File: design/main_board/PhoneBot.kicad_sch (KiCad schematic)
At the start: 37 parts, among them J101 CX70M-24P1, J102 AVR-ISP-6, J103 Conn_02x03_Odd_Even, J104 Conn_02x03_Odd_Even, J105 Conn_02x03_Odd_Even, J106 Conn_02x03_Odd_Even, U101 ATmega32U4-AU, Y101 ABM3-8.000MHZ-D2Y-T

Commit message: Created esp32 footprint and symbol
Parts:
- added U1: ESP32-S3-WROOM-1-N16R8, CustomFootprints:XCVR_ESP32-S3-WROOM-1-N16R8, symbol Custom:ESP32-S3-WROOM-1-N16R8
- R108: value 1k -> 1M; Part https://www.digikey.com/product-detail/en/yageo/RC0603JR-07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 -> https://www.digikey.com/en/products/detail/yageo/RC0603JR-0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
- R109: value 3.6k -> 3.6M; Part https://www.digikey.com/product-detail/en/yageo/RC0402JR-07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 -> https://www.digikey.com/en/products/detail/yageo/RC0603JR-0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
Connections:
- net +3V3: now also U1.2 (3V3), U1.3 (EN)
- net GND: now also U1.1 (GND), U1.40 (GND), U1.41_1 (GND), U1.41_2 (GND), U1.41_3 (GND), U1.41_4 (GND), U1.41_5 (GND), U1.41_6 (GND), U1.41_7 (GND), U1.41_8 (GND), U1.41_9 (GND)
- net ~BLE_RST renamed ~{BLE_RST}
- net ~RST renamed ~{RST}
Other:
- sheet BLESheet ports: added ~{BLE_RST}; removed ~BLE_RST

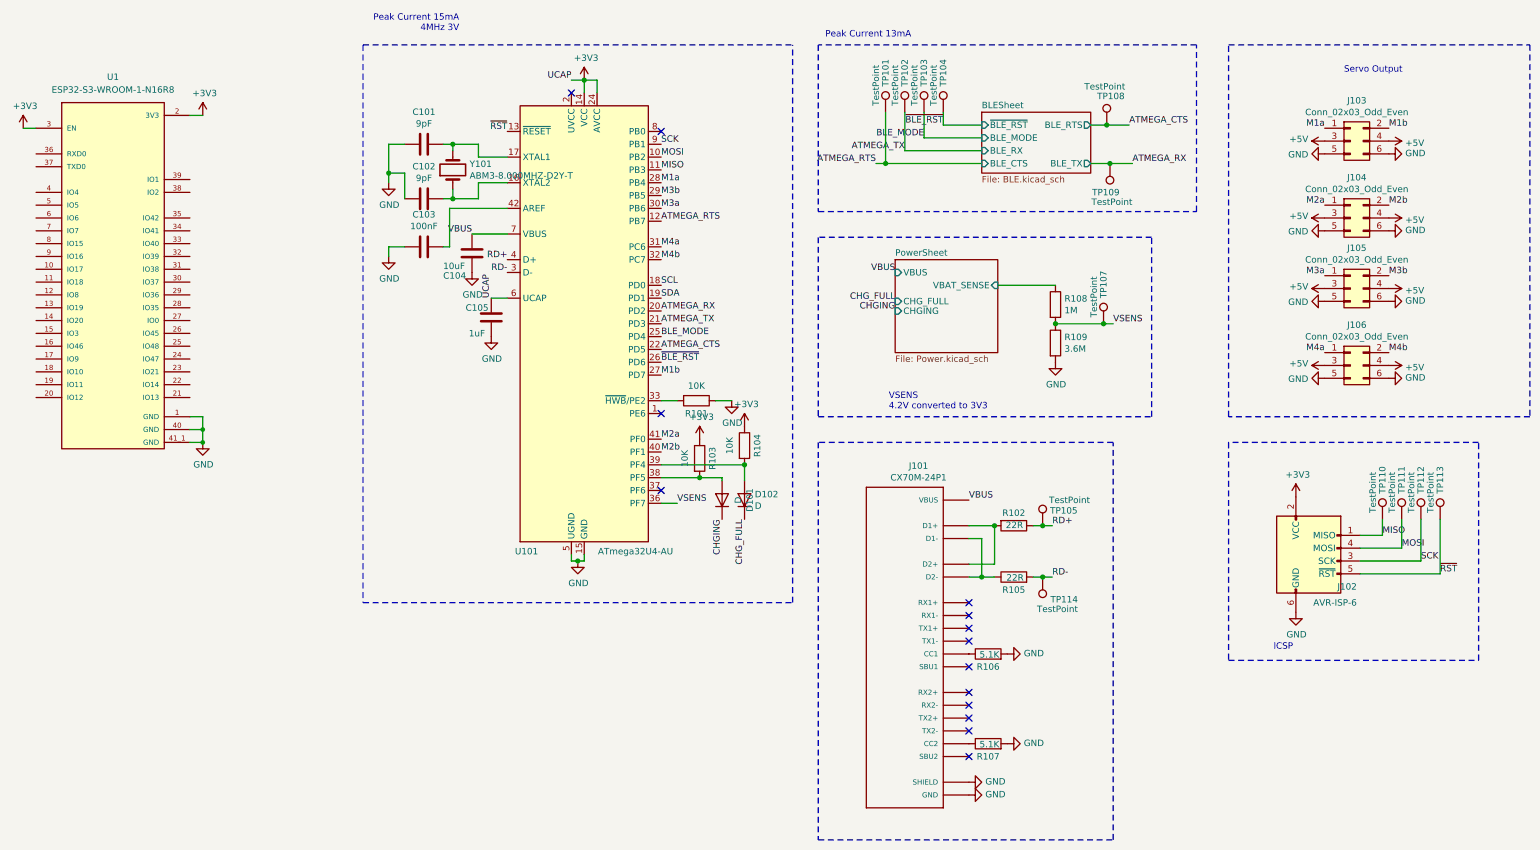
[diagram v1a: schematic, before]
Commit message: Schematic almost finished
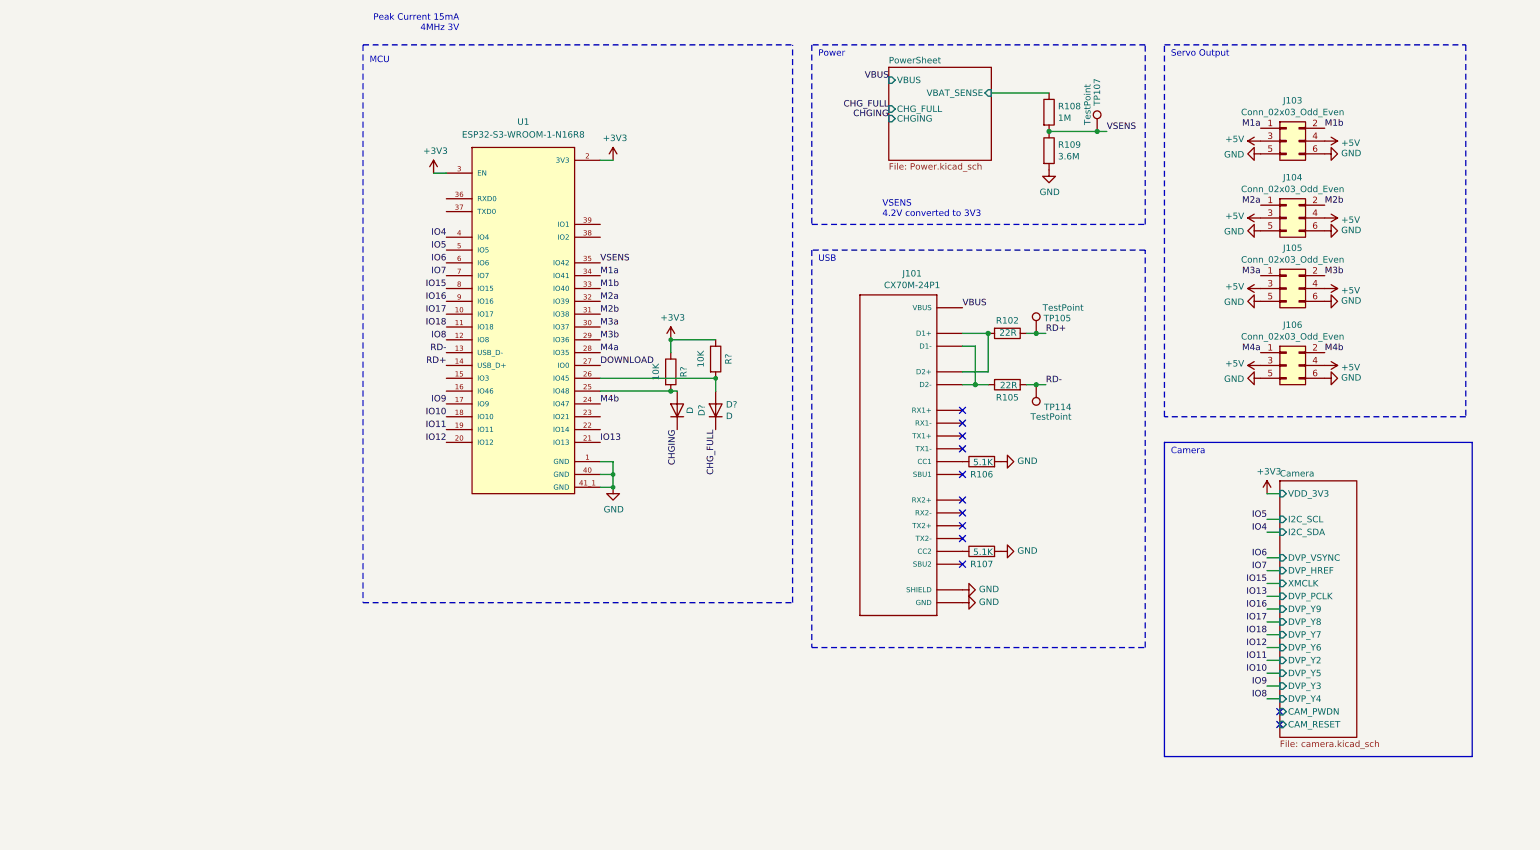
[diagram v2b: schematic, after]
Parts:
- removed C101, C102: 9pF, Capacitor_SMD:C_0603_1608Metric, symbol Device:C
- removed C103: 100nF, Capacitor_SMD:C_0603_1608Metric, symbol Device:C
- removed C104: 10uF, Capacitor_SMD:C_0603_1608Metric, symbol Device:C
- removed C105: 1uF, Capacitor_SMD:C_0603_1608Metric, symbol Device:C
- removed D101, D102: D, Diode_SMD:D_0603_1608Metric, symbol Device:D
- removed J102: AVR-ISP-6, Connector_PinHeader_2.54mm:PinHeader_2x03_P2.54mm_Vertical, symbol PhoneBot-rescue:AVR-ISP-6-Connector-PhoneBot-rescue
- removed R101, R103, R104: 10K, Resistor_SMD:R_0603_1608Metric, symbol Device:R
- removed TP101, TP102, TP103, TP104, TP108, TP109, TP110, TP111, TP112, TP113: TestPoint, TestPoint:TestPoint_Pad_D1.0mm, symbol Connector:TestPoint
- removed U101: ATmega32U4-AU, Package_QFP:TQFP-44_10x10mm_P0.8mm, symbol PhoneBot-rescue:ATmega32U4-AU-MCU_Microchip_ATmega-PhoneBot-rescue-PhoneBot-res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
- removed Y101: ABM3-8.000MHZ-D2Y-T, Crystal:Crystal_SMD_Abracon_ABM3-2Pin_5.0x3.2mm, symbol Device:Crystal
- added D? (x2): D, Diode_SMD:D_0603_1608Metric, symbol Device:D
- added R? (x2): 10K, Resistor_SMD:R_0603_1608Metric, symbol Device:R
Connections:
- net +3V3: now also R?.1, R?.1
- net CHGING: now also D?.1 (K)
- net CHG_FULL: now also D?.1 (K)
- net M1a: now also U1.34 (IO41)
- net M1b: now also U1.33 (IO40)
- net M2a: now also U1.32 (IO39)
- net M2b: now also U1.31 (IO38)
- net M3a: now also U1.30 (IO37)
- net M3b: now also U1.29 (IO36)
- net M4a: now also U1.28 (IO35)
- net M4b: now also U1.24 (IO47)
- net RD+: now also U1.14 (IO20)
- net RD-: now also U1.13 (IO19)
- net VSENS: now also U1.35 (IO42)
- net IO17: now reaches U1.10 (IO17)
- net IO18: now reaches U1.11 (IO18)
- net IO8: now reaches U1.12 (IO8)
- net IO9: now reaches U1.17 (IO9)
- net IO10: now reaches U1.18 (IO10)
- net IO11: now reaches U1.19 (IO11)
- net IO12: now reaches U1.20 (IO12)
- net IO13: now reaches U1.21 (IO13)
- net at U1.25 (IO48): now also D?.2 (A), R?.2
- net at U1.26 (IO45): now also D?.2 (A), R?.2
- net DOWNLOAD: now reaches U1.27 (IO0)
- net IO4: now reaches U1.4 (IO4)
- net IO5: now reaches U1.5 (IO5)
- net IO6: now reaches U1.6 (IO6)
- net IO7: now reaches U1.7 (IO7)
- net IO15: now reaches U1.8 (IO15)
- net IO16: now reaches U1.9 (IO16)
- no-connect marks 14 -> 12
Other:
- removed sheet BLESheet
- added sheet Camera (camera.kicad_sch)
- note added: "Camera"
- note added: "MCU"
- note added: "Power"
- note added: "USB"
- note removed: "ICSP"
- note removed: "Peak Current 13mA"
- moved on the sheet: J101, J103, J104, J105, J106, R102, R105, R106, R107, R108, R109, TP105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

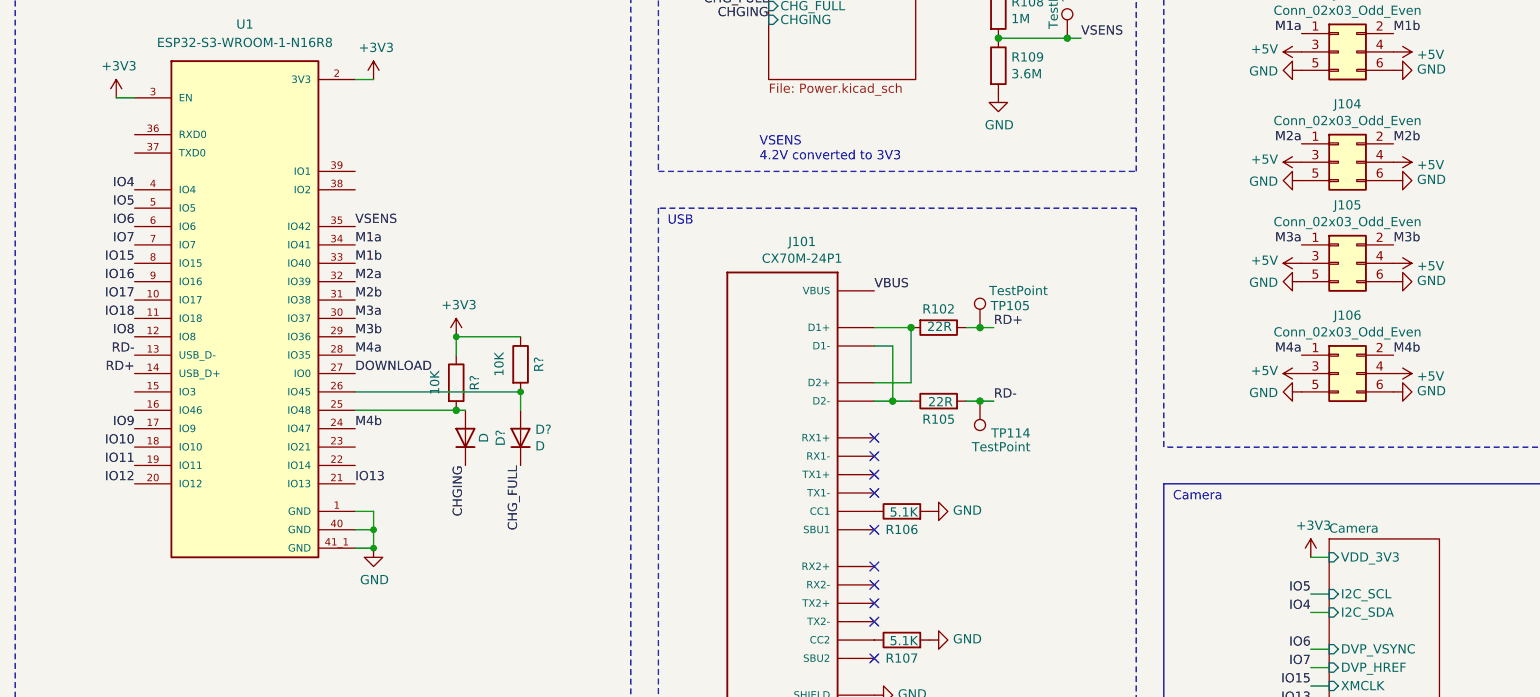
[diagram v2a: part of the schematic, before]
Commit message: Added new firmware hello world for ESP32-S3
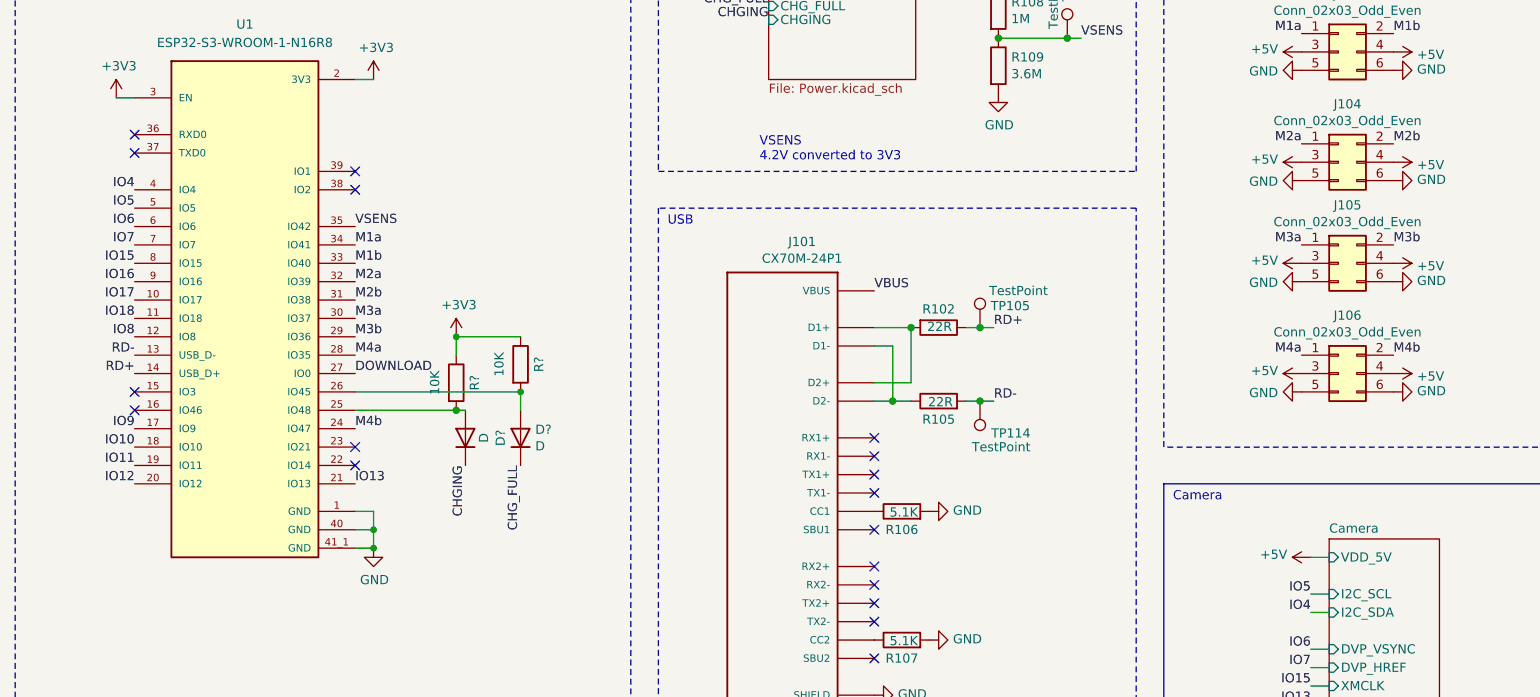
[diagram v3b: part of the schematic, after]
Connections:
- no-connect marks 12 -> 20
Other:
- sheet Camera ports: added VDD_5V; removed VDD_3V3
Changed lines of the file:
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@@
   (no_connect (at 137.795 127))
   (no_connect (at 137.795 114.3))
+  (no_connect (at 66.04 97.79))
+  (no_connect (at 66.04 100.33))
+  (no_connect (at 35.56 90.17))
+  (no_connect (at 35.56 92.71))
+  (no_connect (at 35.56 57.15))
+  (no_connect (at 35.56 54.61))
+  (no_connect (at 66.04 62.23))
+  (no_connect (at 66.04 59.69))
   (no_connect (at 137.795 104.14))
   (no_connect (at 137.795 96.52))
@@
     (pin "2")
   )
-  (symbol (lib_id "power:+3V3") (at 198.12 113.03 0) (unit 1)
-    (in_bom yes) (on_board yes)
-    (property "Reference" "#PWR?" (id 0) (at 198.12 116.84 0)
-      (effects (font (size 1.27 1.27)) hide)
-    )
-    (property "Value" "+3V3" (id 1) (at 198.501 108.6358 0))
-    (property "Footprint" "" (id 2) (at 198.12 113.03 0)
-      (effects (font (size 1.27 1.27)) hide)
-    )
-    (property "Datasheet" "" (id 3) (at 198.12 113.03 0)
-      (effects (font (size 1.27 1.27)) hide)
-    )
-    (pin "1")
-  )
   (symbol (lib_id "Device:D") (at 81.28 96.52 90) (unit 1)
     (in_bom yes) (on_board yes)
@@
     )
     (property "Datasheet" "" (id 3) (at 33.02 49.53 0)
+      (effects (font (size 1.27 1.27)) hide)
+    )
+    (pin "1")
+  )
+  (symbol (lib_id "power:+5V") (at 198.12 113.03 90) (unit 1)
+    (in_bom yes) (on_board yes)
+    (property "Reference" "#PWR?" (id 0) (at 201.93 113.03 0)
+      (effects (font (size 1.27 1.27)) hide)
+    )
+    (property "Value" "+5V" (id 1) (at 194.8688 112.649 90)
+      (effects (font (size 1.27 1.27)) (justify left))
+    )
+    (property "Footprint" "" (id 2) (at 198.12 113.03 0)
+      (effects (font (size 1.27 1.27)) hide)
+    )
+    (property "Datasheet" "" (id 3) (at 198.12 113.03 0)
       (effects (font (size 1.27 1.27)) hide)
     )
@@
       (effects (font (size 1.27 1.27)) (justify left))
     )
-    (pin "VDD_3V3" input (at 200.66 113.03 180)
+    (pin "VDD_5V" input (at 200.66 113.03 180)
       (effects (font (size 1.27 1.27)) (justify left))
     )
@@
       (reference "#PWR0323") (unit 1) (value "GND") (footprint "")
     )
-    (path "/fb076d76-cc09-41e3-aa25-fa50a03831fa/0cceaf40-9824-4e98-9a59-b5b2d1f7687e"
-      (reference "#PWR?") (unit 1) (value "GND") (footprint "")
-    )
     (path "/fb076d76-cc09-41e3-aa25-fa50a03831fa/0e34cb7b-a544-4e7f-a839-0010927047ca"
       (reference "#PWR?") (unit 1) (value "GND") (footprint "")
     )
-    (path "/1c51eb0b-fc14-4ea2-b61c-048e1f6bf0ce"
-      (reference "#PWR?") (unit 1) (value "+3V3") (footprint "")
-    )
     (path "/fb076d76-cc09-41e3-aa25-fa50a03831fa/1d7af2fb-9312-4ce2-9df7-62fb6ef2fa26"
       (reference "#PWR?") (unit 1) (value "GND") (footprint "")
@@
       (reference "#PWR?") (unit 1) (value "+3V3") (footprint "")
     )
-    (path "/fb076d76-cc09-41e3-aa25-fa50a03831fa/46b31701-821c-4d3a-81dd-d9dd67d22395"
-      (reference "#PWR?") (unit 1) (value "GND") (footprint "")
-    )
     (path "/fb076d76-cc09-41e3-aa25-fa50a03831fa/475ce8d9-c2d9-4f52-852b-2da774ed9281"
       (reference "#PWR?") (unit 1) (value "GND") (footprint "")
@@
       (reference "#PWR?") (unit 1) (value "GND") (footprint "")
     )
-    (path "/fb076d76-cc09-41e3-aa25-fa50a03831fa/c19564cd-c14e-46f5-9427-2ee713825ce0"
-      (reference "#PWR?") (unit 1) (value "GND") (footprint "")
-    )
-    (path "/fb076d76-cc09-41e3-aa25-fa50a03831fa/cba08101-79ff-4a00-9775-67531e5efcf0"
-      (reference "#PWR?") (unit 1) (value "GND") (footprint "")
+    (path "/d17d153e-880f-46f7-8a47-dfb469371111"
+      (reference "#PWR?") (unit 1) (value "+5V") (footprint "")
     )
     (path "/fb076d76-cc09-41e3-aa25-fa50a03831fa/d78d573e-cde6-4a68-a2b9-97967007fbe8"
@@
       (reference "#PWR?") (unit 1) (value "GND") (footprint "")
     )
-    (path "/fb076d76-cc09-41e3-aa25-fa50a03831fa/edb1327f-b177-4c6f-9c0f-9d70ef7a9e8b"
-      (reference "#PWR?") (unit 1) (value "GND") (footprint "")
-    )
     (path "/fb076d76-cc09-41e3-aa25-fa50a03831fa/ee034719-8556-4aa1-8e9a-64f92e5cef0e"
       (reference "#PWR?") (unit 1) (value "GND") (footprint "")
@@
       (reference "C?") (unit 1) (value "0.1uF") (footprint "")
     )
-    (path "/fb076d76-cc09-41e3-aa25-fa50a03831fa/395c01ef-25bf-4381-a4aa-39671e8e2524"
-      (reference "C?") (unit 1) (value "0.1uF") (footprint "")
-    )
     (path "/fb076d76-cc09-41e3-aa25-fa50a03831fa/581e088f-6980-477d-ab85-536c5503921d"
       (reference "C?") (unit 1) (value "0.1uF") (footprint "")
     )
-    (path "/fb076d76-cc09-41e3-aa25-fa50a03831fa/6615c85d-01b1-455d-9f4c-8b1bfbb011e2"
-      (reference "C?") (unit 1) (value "4.7uF") (footprint "")
-    )
-    (path "/fb076d76-cc09-41e3-aa25-fa50a03831fa/69d6e3af-ebb1-4f7d-a706-f3a91ab2267a"
-      (reference "C?") (unit 1) (value "4.7uF") (footprint "")
-    )
     (path "/fb076d76-cc09-41e3-aa25-fa50a03831fa/88a6ab3c-510e-432b-9074-7a680b804db5"
       (reference "C?") (unit 1) (value "10uF") (footprint "")
     )
-    (path "/fb076d76-cc09-41e3-aa25-fa50a03831fa/9b274e07-3463-4390-aa68-6b54be69f0cf"
-      (reference "C?") (unit 1) (value "0.1uF") (footprint "")
-    )
     (path "/fb076d76-cc09-41e3-aa25-fa50a03831fa/9da4e42c-1c00-4f12-a697-13b6c872b34e"
       (reference "C?") (unit 1) (value "10uF") (footprint "")
@@
       (reference "C?") (unit 1) (value "10uF") (footprint "")
     )
-    (path "/fb076d76-cc09-41e3-aa25-fa50a03831fa/be728978-e3f4-4ce3-a0cd-93ba032850e1"
-      (reference "C?") (unit 1) (value "4.7uF") (footprint "")
-    )
     (path "/fb076d76-cc09-41e3-aa25-fa50a03831fa/c4ce2d0a-d024-4c63-904e-0471b83406ef"
